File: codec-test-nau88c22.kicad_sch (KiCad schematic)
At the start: 74 parts, among them J1 Conn_01x03_Male, J10 AudioJack3, J11 Conn_01x02_Male, J2 Conn_01x03_Male, J3 Conn_02x05_Odd_Even, J4 Conn_02x04_Odd_Even, J5 AudioJack3, J6 AudioJack3, J7 AudioJack3, J8 AudioJack2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

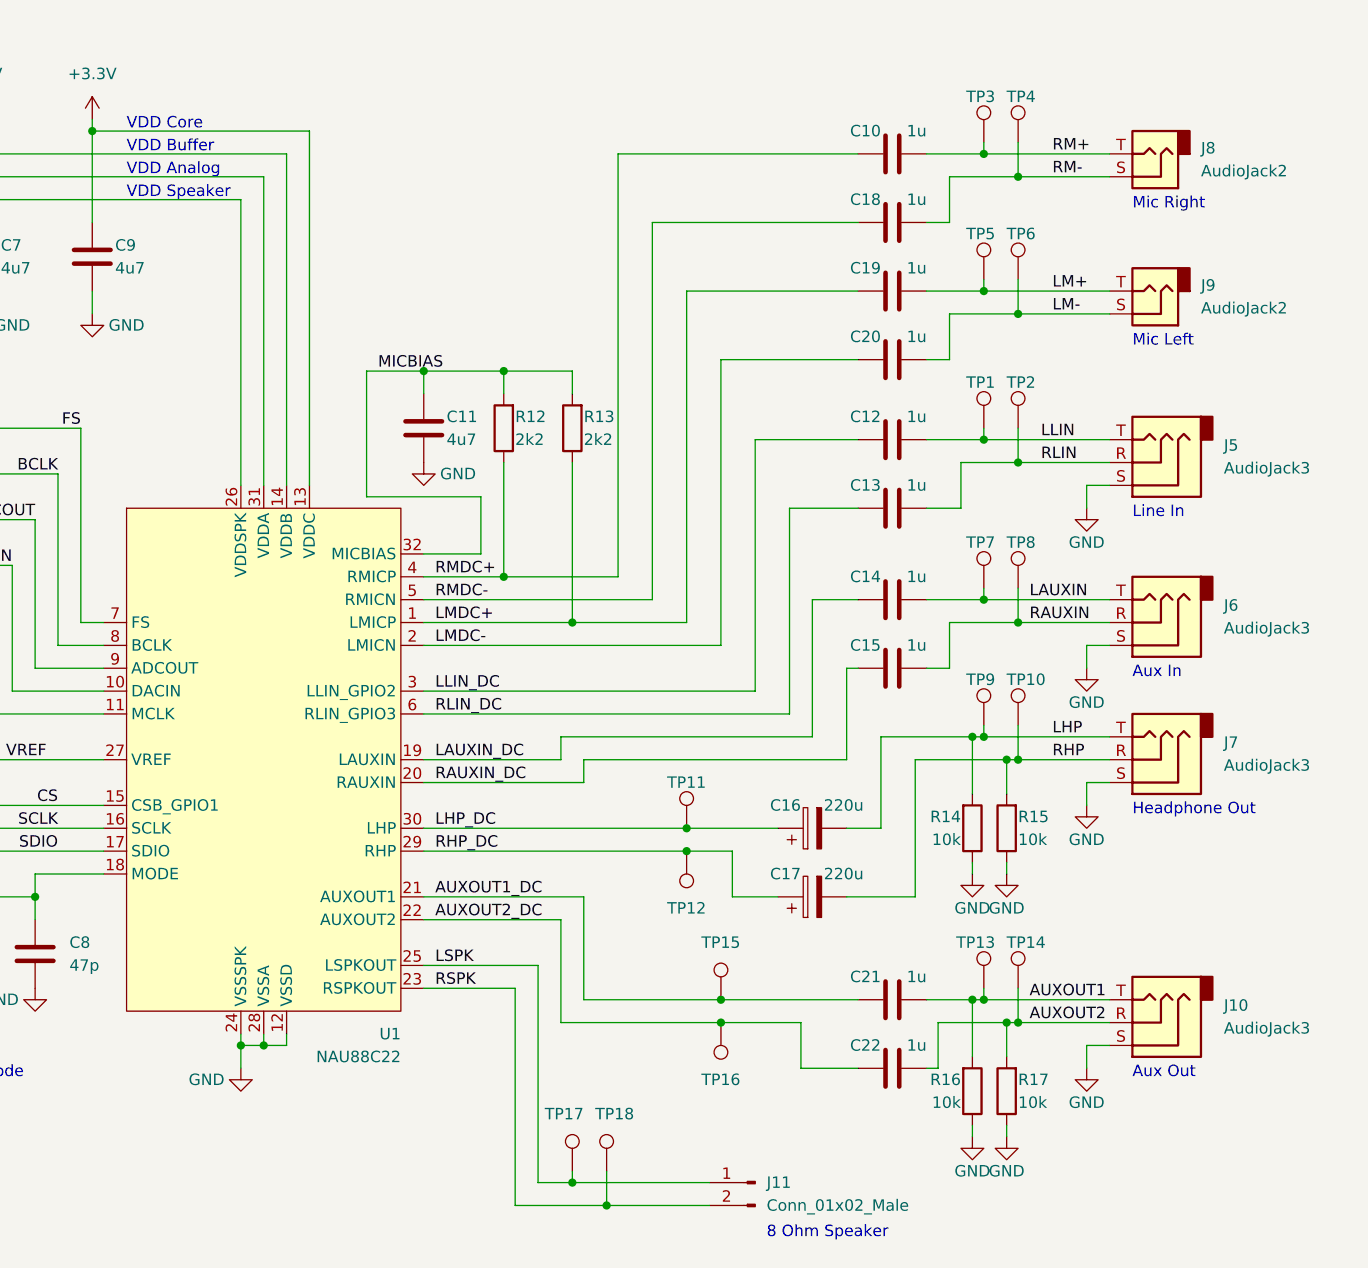
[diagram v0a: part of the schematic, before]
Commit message: Rewired then updated kibot
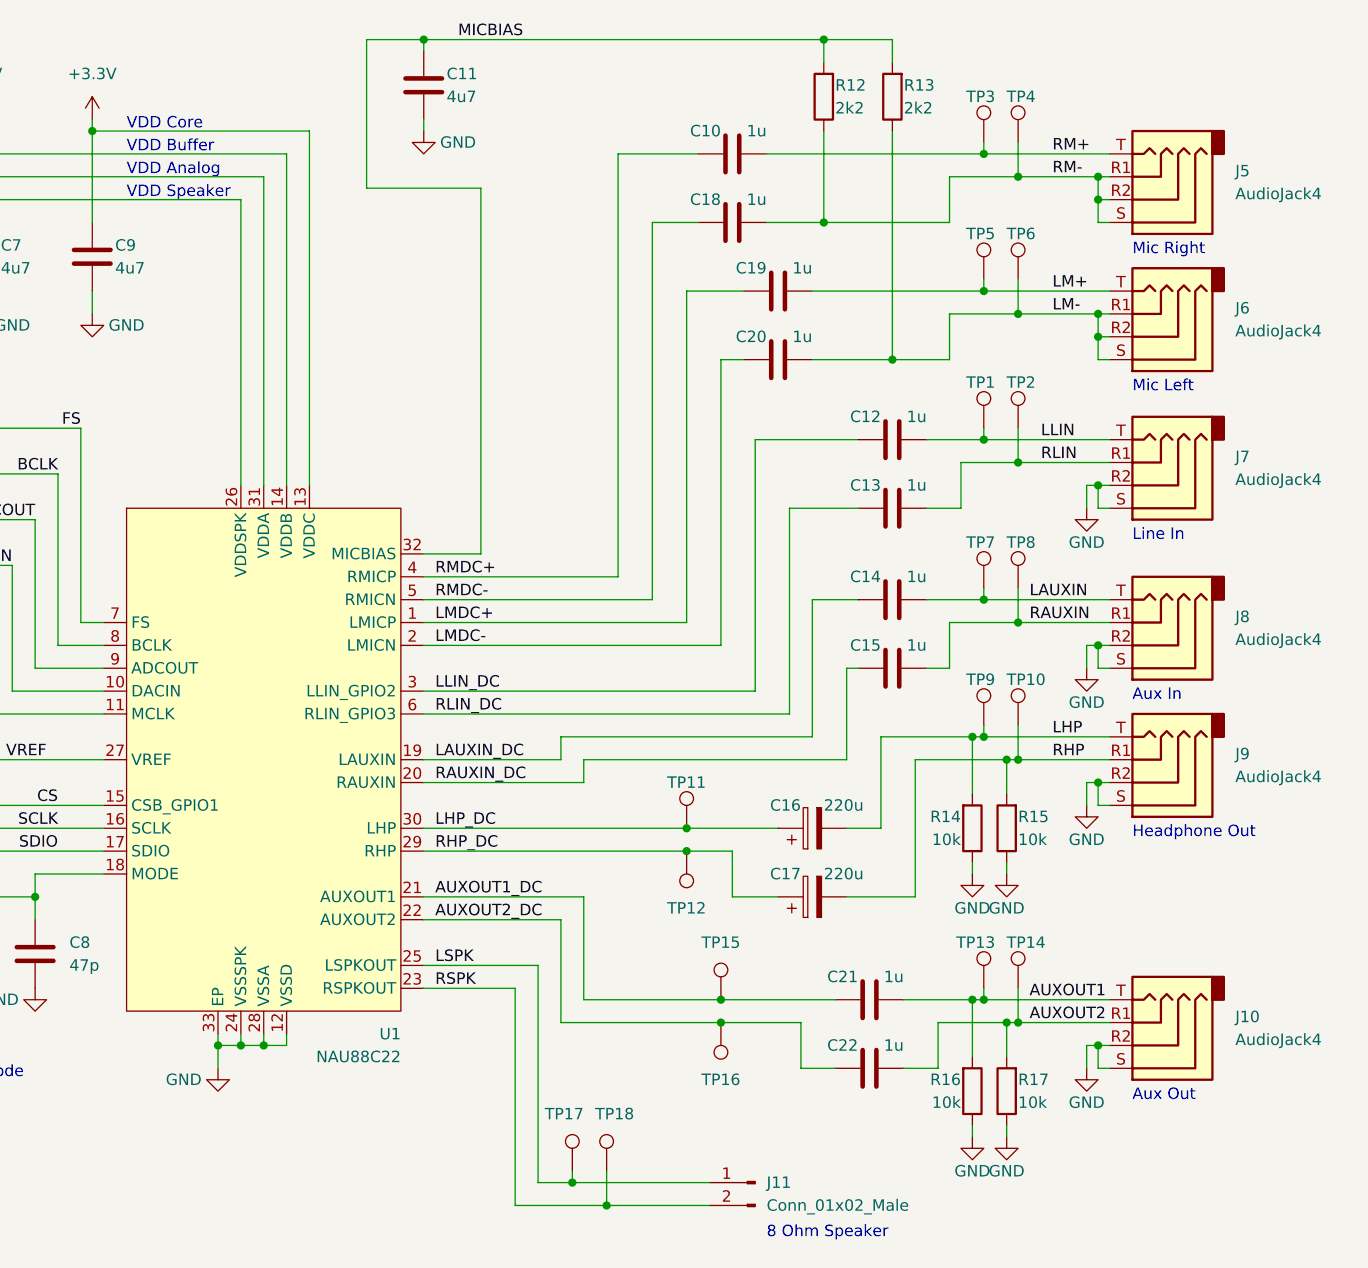
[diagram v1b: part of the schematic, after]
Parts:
- removed J10, J5, J6, J7: AudioJack3, Connector_Audio:Jack_3.5mm_PJ320D_Horizontal, symbol Connector:AudioJack3
- removed J8, J9: AudioJack2, Connector_Audio:Jack_3.5mm_PJ320D_Horizontal, symbol Connector:AudioJack2
- added J10, J5, J6, J7, J8, J9: AudioJack4, Connector_Audio:Jack_3.5mm_PJ320D_Horizontal, symbol Connector:AudioJack4
- C1, C3, C6, C8: JLCPCB C14857 -> (none); Manufacturer (none) -> Samsung
- C10, C12, C13, C14, C15, C18, C19, C20, C21, C22: JLCPCB C28323 -> (none); Manufacturer (none) -> Samsung
- C11, C2, C4, C5, C7, C9: JLCPCB C1779 -> (none); Manufacturer (none) -> Samsung
- C16, C17: JLCPCB C125977 -> (none); Manufacturer (none) -> Nichicon
- R1, R10, R2, R3, R4, R5, R6, R7, R8, R9: JLCPCB C17557 -> (none); Manufacturer (none) -> Uni-royal
- R11: JLCPCB C17477 -> (none); Manufacturer (none) -> Uni-royal
- R12, R13: JLCPCB C17520 -> (none); Manufacturer (none) -> Uni-royal
- R14, R15, R16, R17: JLCPCB C17414 -> (none); Manufacturer (none) -> Uni-royal
- U1: JLCPCB C914209 -> (none); Manufacturer (none) -> Nuvoton
- X1: JLCPCB C5203546 -> (none); Manufacturer (none) -> YXC
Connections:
- net AUXOUT1: now also J10.T
- net AUXOUT2: now also J10.R1
- net GND: now also U1.33 (EP), J10.R2, J10.S, J7.R2, J7.S, J8.R2, J8.S, J9.R2, J9.S
- net LAUXIN: now also J8.T
- net LHP: now also J9.T
- net LLIN: now also J7.T
- net LM+: now also J6.T
- net LM-: now also R13.1, J6.R1, J6.R2, J6.S
- net LMDC+: no longer R13.1
- net RAUXIN: now also J8.R1
- net RHP: now also J9.R1
- net RLIN: now also J7.R1
- net RM+: now also J5.T
- net RM-: now also R12.1, J5.R1, J5.R2, J5.S
- net RMDC+: no longer R12.1
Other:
- company: (none) -> github.com/neotron-compute/codec-test-nau88c22
- title: (none) -> Codec Test NAU88C22 
- moved on the sheet: C10, C11, C18, C19, C20, C21, C22, R12, R13
